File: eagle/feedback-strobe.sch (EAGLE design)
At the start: 17 parts, among them J2 MOTOR, U1 74LCX760SOIC20, U2 +12v, U3 V_REG_317SMD

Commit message: finished v1 PCB design
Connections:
- net GND: now also U1./OE1, U1./OE2
- net LED1: now also R4.2; no longer R1.2
- net LED2: now also R3.2; no longer R2.2
- net LED3: now also R2.2; no longer R3.2
- net LED4: now also R1.2; no longer R4.2
- net LED5: now also R8.2; no longer R5.2
- net LED6: now also R7.2; no longer R6.2
- net LED7: now also R6.2; no longer R7.2
- net LED8: now also R5.2; no longer R8.2
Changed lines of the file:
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@@
 <part name="C1" library="SparkFun-Passives" deviceset="CAP_POL" device="F80" value="220uF"/>
 <part name="GND3" library="SparkFun-Aesthetics" deviceset="GND" device=""/>
+<part name="GND4" library="SparkFun-Aesthetics" deviceset="GND" device=""/>
+<part name="GND5" library="SparkFun-Aesthetics" deviceset="GND" device=""/>
 </parts>
 <sheets>
@@
 <instance part="C1" gate="G$1" x="5.08" y="116.84"/>
 <instance part="GND3" gate="1" x="-35.56" y="104.14"/>
+<instance part="GND4" gate="1" x="-2.54" y="116.84"/>
+<instance part="GND5" gate="1" x="76.2" y="104.14"/>
 </instances>
 <busses>
@@
 <wire x1="15.24" y1="119.38" x2="15.24" y2="109.22" width="0.1524" layer="91"/>
 <wire x1="15.24" y1="109.22" x2="5.08" y2="109.22" width="0.1524" layer="91"/>
-<pinref part="DC_IN" gate="G$1" pin="GNDBREAK"/>
 <pinref part="DC_IN" gate="G$1" pin="GND"/>
-<wire x1="5.08" y1="109.22" x2="0" y2="109.22" width="0.1524" layer="91"/>
-<wire x1="-10.16" y1="124.46" x2="-10.16" y2="121.92" width="0.1524" layer="91"/>
-<wire x1="-10.16" y1="121.92" x2="0" y2="121.92" width="0.1524" layer="91"/>
-<wire x1="0" y1="121.92" x2="0" y2="109.22" width="0.1524" layer="91"/>
-<junction x="0" y="109.22"/>
+<wire x1="5.08" y1="109.22" x2="-7.62" y2="109.22" width="0.1524" layer="91"/>
+<wire x1="-10.16" y1="121.92" x2="-7.62" y2="121.92" width="0.1524" layer="91"/>
+<wire x1="-7.62" y1="121.92" x2="-7.62" y2="109.22" width="0.1524" layer="91"/>
+<junction x="-7.62" y="109.22"/>
 <pinref part="C1" gate="G$1" pin="-"/>
 <wire x1="5.08" y1="111.76" x2="5.08" y2="109.22" width="0.1524" layer="91"/>
 <junction x="5.08" y="109.22"/>
 <pinref part="GND3" gate="1" pin="GND"/>
-<wire x1="0" y1="109.22" x2="-35.56" y2="109.22" width="0.1524" layer="91"/>
+<wire x1="-7.62" y1="109.22" x2="-35.56" y2="109.22" width="0.1524" layer="91"/>
 <wire x1="-35.56" y1="109.22" x2="-35.56" y2="106.68" width="0.1524" layer="91"/>
 </segment>
@@
 <pinref part="GND2" gate="1" pin="GND"/>
 <wire x1="27.94" y1="73.66" x2="27.94" y2="68.58" width="0.1524" layer="91"/>
+</segment>
+<segment>
+<pinref part="DC_IN" gate="G$1" pin="GNDBREAK"/>
+<pinref part="GND4" gate="1" pin="GND"/>
+<wire x1="-10.16" y1="124.46" x2="-2.54" y2="124.46" width="0.1524" layer="91"/>
+<wire x1="-2.54" y1="124.46" x2="-2.54" y2="119.38" width="0.1524" layer="91"/>
+</segment>
+<segment>
+<pinref part="U1" gate="U1" pin="/OE2"/>
+<wire x1="58.42" y1="93.98" x2="68.58" y2="93.98" width="0.1524" layer="91"/>
+<wire x1="68.58" y1="93.98" x2="68.58" y2="111.76" width="0.1524" layer="91"/>
+<wire x1="68.58" y1="111.76" x2="25.4" y2="111.76" width="0.1524" layer="91"/>
+<wire x1="25.4" y1="111.76" x2="25.4" y2="99.06" width="0.1524" layer="91"/>
+<pinref part="U1" gate="U1" pin="/OE1"/>
+<wire x1="25.4" y1="99.06" x2="27.94" y2="99.06" width="0.1524" layer="91"/>
+<wire x1="68.58" y1="111.76" x2="76.2" y2="111.76" width="0.1524" layer="91"/>
+<wire x1="76.2" y1="111.76" x2="76.2" y2="106.68" width="0.1524" layer="91"/>
+<pinref part="GND5" gate="1" pin="GND"/>
 </segment>
 </net>
@@
 <net name="LED1" class="0">
 <segment>
-<pinref part="R1" gate="G$1" pin="2"/>
-<wire x1="-22.86" y1="81.28" x2="-7.62" y2="81.28" width="0.1524" layer="91"/>
-</segment>
-<segment>
 <pinref part="U1" gate="U1" pin="O_0"/>
 <wire x1="58.42" y1="91.44" x2="63.5" y2="91.44" width="0.1524" layer="91"/>
 <label x="63.5" y="91.44" size="1.778" layer="95"/>
 </segment>
+<segment>
+<pinref part="R4" gate="G$1" pin="2"/>
+<wire x1="-12.7" y1="73.66" x2="-7.62" y2="73.66" width="0.1524" layer="91"/>
+</segment>
 </net>
 <net name="N$3" class="0">
@@
 <net name="LED2" class="0">
 <segment>
-<pinref part="R2" gate="G$1" pin="2"/>
-<wire x1="-12.7" y1="78.74" x2="-7.62" y2="78.74" width="0.1524" layer="91"/>
-</segment>
-<segment>
 <pinref part="U1" gate="U1" pin="O_1"/>
 <wire x1="58.42" y1="86.36" x2="63.5" y2="86.36" width="0.1524" layer="91"/>
 <label x="63.5" y="86.36" size="1.778" layer="95"/>
 </segment>
+<segment>
+<pinref part="R3" gate="G$1" pin="2"/>
+<wire x1="-22.86" y1="76.2" x2="-7.62" y2="76.2" width="0.1524" layer="91"/>
+</segment>
 </net>
 <net name="N$5" class="0">
@@
 <net name="LED3" class="0">
 <segment>
-<pinref part="R3" gate="G$1" pin="2"/>
-<wire x1="-22.86" y1="76.2" x2="-7.62" y2="76.2" width="0.1524" layer="91"/>
-</segment>
-<segment>
 <pinref part="U1" gate="U1" pin="O_2"/>
 <wire x1="58.42" y1="81.28" x2="63.5" y2="81.28" width="0.1524" layer="91"/>
 <label x="63.5" y="81.28" size="1.778" layer="95"/>
 </segment>
+<segment>
+<pinref part="R2" gate="G$1" pin="2"/>
+<wire x1="-12.7" y1="78.74" x2="-7.62" y2="78.74" width="0.1524" layer="91"/>
+</segment>
 </net>
 <net name="LED4" class="0">
-<segment>
-<pinref part="R4" gate="G$1" pin="2"/>
-<wire x1="-12.7" y1="73.66" x2="-7.62" y2="73.66" width="0.1524" layer="91"/>
-</segment>
 <segment>
 <pinref part="U1" gate="U1" pin="O_3"/>
@@
 <label x="63.5" y="76.2" size="1.778" layer="95"/>
 </segment>
+<segment>
+<pinref part="R1" gate="G$1" pin="2"/>
+<wire x1="-22.86" y1="81.28" x2="-7.62" y2="81.28" width="0.1524" layer="91"/>
+</segment>
 </net>
 <net name="LED6" class="0">
-<segment>
-<pinref part="R6" gate="G$1" pin="2"/>
-<wire x1="-12.7" y1="68.58" x2="-7.62" y2="68.58" width="0.1524" layer="91"/>
-</segment>
 <segment>
 <pinref part="U1" gate="U1" pin="O_5"/>
@@
 <label x="17.78" y="88.9" size="1.778" layer="95"/>
 </segment>
+<segment>
+<pinref part="R7" gate="G$1" pin="2"/>
+<wire x1="-22.86" y1="66.04" x2="-7.62" y2="66.04" width="0.1524" layer="91"/>
+</segment>
 </net>
 <net name="LED8" class="0">
-<segment>
-<pinref part="R8" gate="G$1" pin="2"/>
-<wire x1="-12.7" y1="63.5" x2="-7.62" y2="63.5" width="0.1524" layer="91"/>
-</segment>
 <segment>
 <pinref part="U1" gate="U1" pin="O_7"/>
@@
 <label x="17.78" y="78.74" size="1.778" layer="95"/>
 </segment>
+<segment>
+<pinref part="R5" gate="G$1" pin="2"/>
+<wire x1="-22.86" y1="71.12" x2="-7.62" y2="71.12" width="0.1524" layer="91"/>
+</segment>
 </net>
 <net name="N$12" class="0">
@@
 <net name="LED7" class="0">
 <segment>
-<pinref part="R7" gate="G$1" pin="2"/>
-<wire x1="-22.86" y1="66.04" x2="-7.62" y2="66.04" width="0.1524" layer="91"/>
-</segment>
-<segment>
 <pinref part="U1" gate="U1" pin="O_6"/>
 <wire x1="22.86" y1="83.82" x2="27.94" y2="83.82" width="0.1524" layer="91"/>
 <label x="17.78" y="83.82" size="1.778" layer="95"/>
 </segment>
+<segment>
+<pinref part="R6" gate="G$1" pin="2"/>
+<wire x1="-12.7" y1="68.58" x2="-7.62" y2="68.58" width="0.1524" layer="91"/>
+</segment>
 </net>
 <net name="LED5" class="0">
-<segment>
-<pinref part="R5" gate="G$1" pin="2"/>
-<wire x1="-7.62" y1="71.12" x2="-22.86" y2="71.12" width="0.1524" layer="91"/>
-</segment>
 <segment>
 <pinref part="U1" gate="U1" pin="O_4"/>
@@
 <label x="17.78" y="93.98" size="1.778" layer="95"/>
 </segment>
-</net>
+<segment>
+<pinref part="R8" gate="G$1" pin="2"/>
+<wire x1="-12.7" y1="63.5" x2="-7.62" y2="63.5" width="0.1524" layer="91"/>
+</segment>
+</net>

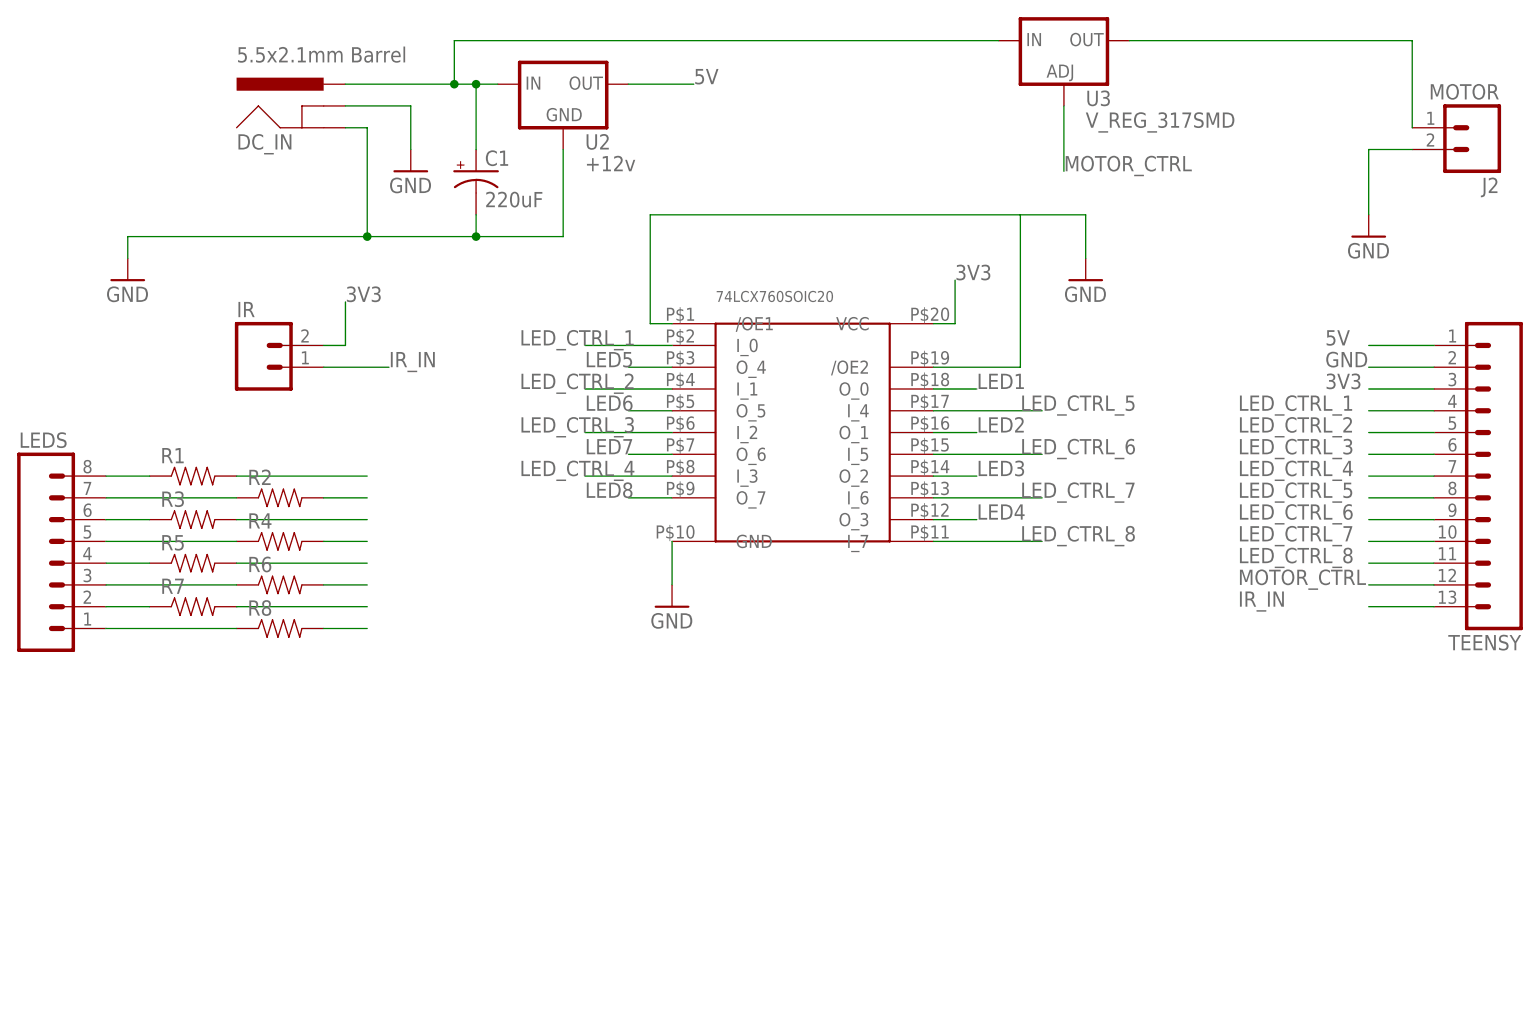
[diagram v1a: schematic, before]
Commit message: edited mosfet label
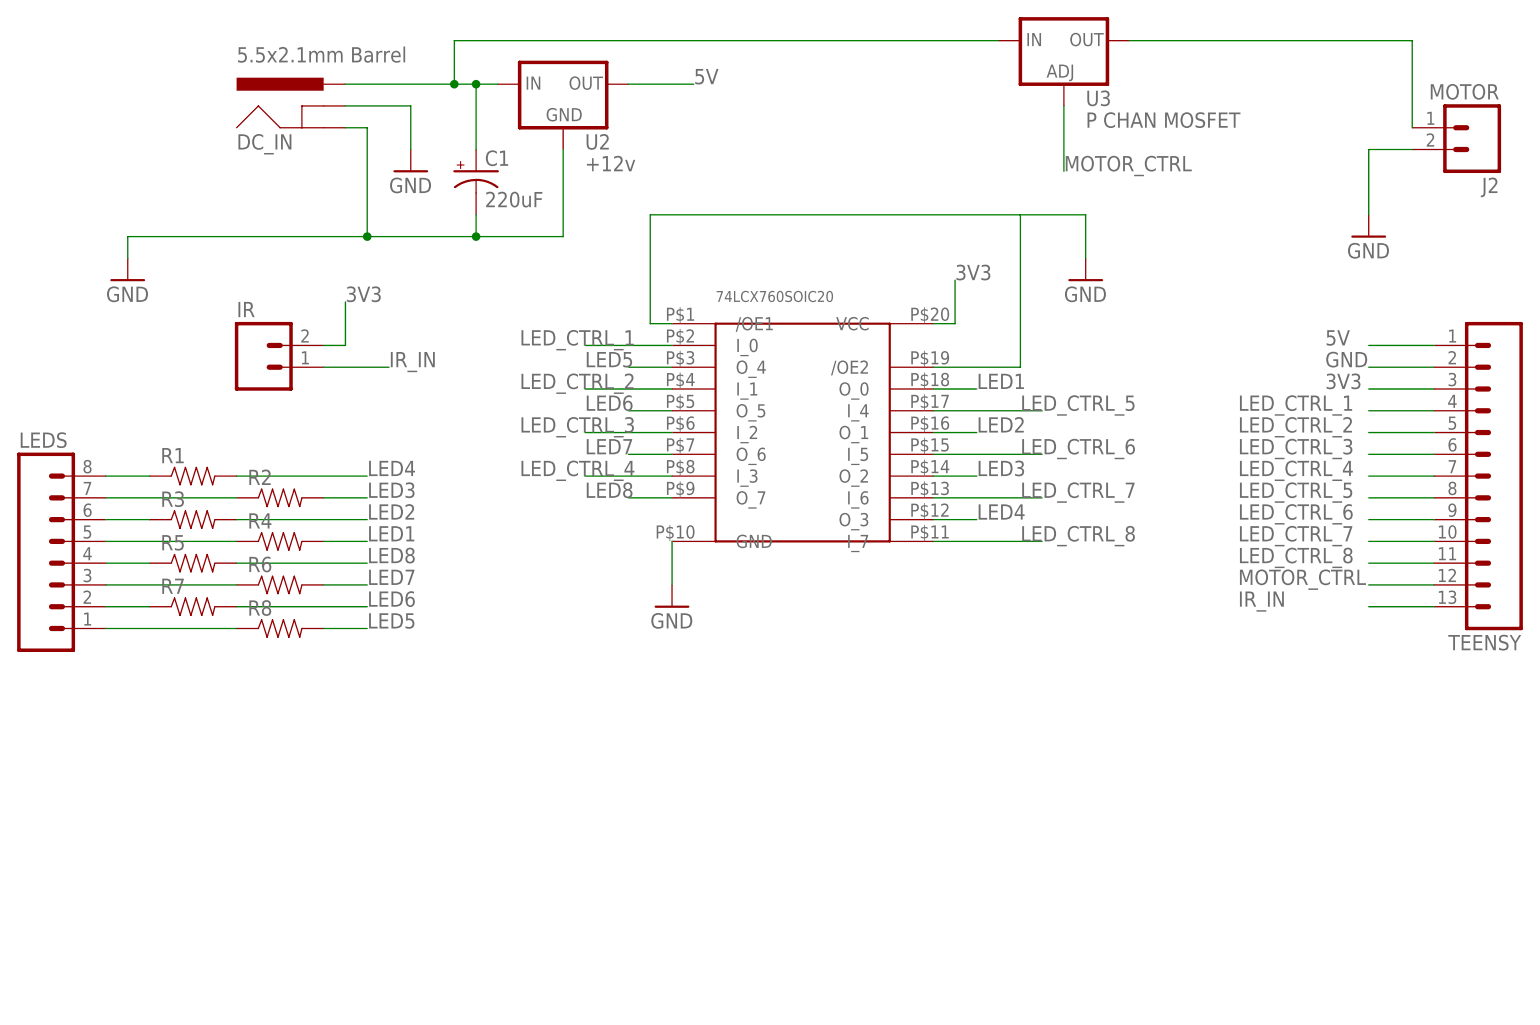
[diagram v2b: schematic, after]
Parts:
- U3: value V_REG_317SMD -> P CHAN MOSFET
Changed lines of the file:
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@@
 <part name="U1" library="SparkFun-DigitalIC" deviceset="74LCX760" device="SOIC20"/>
 <part name="U2" library="SparkFun-PowerIC" deviceset="V_REG_78XX" device="7812" value="+12v"/>
-<part name="U3" library="SparkFun-PowerIC" deviceset="V_REG_317" device="SMD"/>
+<part name="U3" library="SparkFun-PowerIC" deviceset="V_REG_317" device="SMD" value="P CHAN MOSFET"/>
 <part name="GND1" library="SparkFun-Aesthetics" deviceset="GND" device=""/>
 <part name="TEENSY" library="SparkFun-Connectors" deviceset="M13" device=""/>
@@
 <pinref part="R4" gate="G$1" pin="2"/>
 <wire x1="-12.7" y1="73.66" x2="-7.62" y2="73.66" width="0.1524" layer="91"/>
+<label x="-7.62" y="73.66" size="1.778" layer="95"/>
 </segment>
 </net>
@@
 <pinref part="R3" gate="G$1" pin="2"/>
 <wire x1="-22.86" y1="76.2" x2="-7.62" y2="76.2" width="0.1524" layer="91"/>
+<label x="-7.62" y="76.2" size="1.778" layer="95"/>
 </segment>
 </net>
@@
 <pinref part="R2" gate="G$1" pin="2"/>
 <wire x1="-12.7" y1="78.74" x2="-7.62" y2="78.74" width="0.1524" layer="91"/>
+<label x="-7.62" y="78.74" size="1.778" layer="95"/>
 </segment>
 </net>
@@
 <pinref part="R1" gate="G$1" pin="2"/>
 <wire x1="-22.86" y1="81.28" x2="-7.62" y2="81.28" width="0.1524" layer="91"/>
+<label x="-7.62" y="81.28" size="1.778" layer="95"/>
 </segment>
 </net>
@@
 <pinref part="R7" gate="G$1" pin="2"/>
 <wire x1="-22.86" y1="66.04" x2="-7.62" y2="66.04" width="0.1524" layer="91"/>
+<label x="-7.62" y="66.04" size="1.778" layer="95"/>
 </segment>
 </net>
@@
 <pinref part="R5" gate="G$1" pin="2"/>
 <wire x1="-22.86" y1="71.12" x2="-7.62" y2="71.12" width="0.1524" layer="91"/>
+<label x="-7.62" y="71.12" size="1.778" layer="95"/>
 </segment>
 </net>
@@
 <pinref part="R6" gate="G$1" pin="2"/>
 <wire x1="-12.7" y1="68.58" x2="-7.62" y2="68.58" width="0.1524" layer="91"/>
+<label x="-7.62" y="68.58" size="1.778" layer="95"/>
 </segment>
 </net>
@@
 <pinref part="R8" gate="G$1" pin="2"/>
 <wire x1="-12.7" y1="63.5" x2="-7.62" y2="63.5" width="0.1524" layer="91"/>
-</segment>
-</net>
+<label x="-7.62" y="63.5" size="1.778" layer="95"/>
+</segment>
+</net>

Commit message: new components added, new board dimensions set. routing started. mosfet footprint from digikey not wanting to connect nets
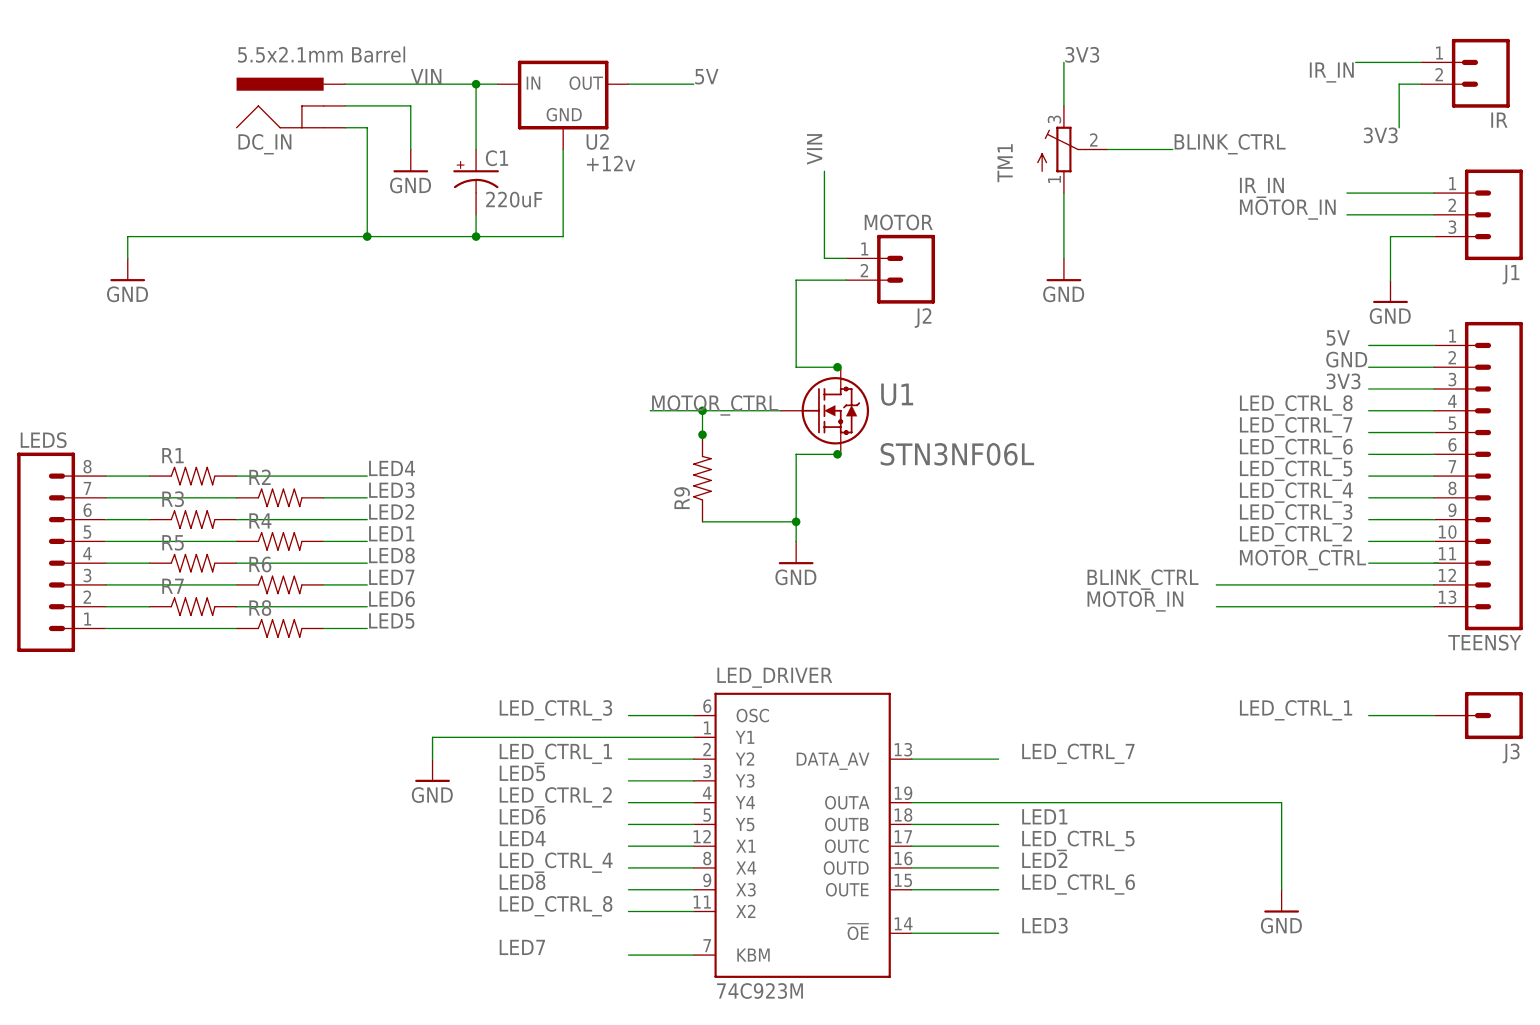
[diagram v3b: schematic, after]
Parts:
- removed U3: P CHAN MOSFET, SparkFun-PowerIC:V_REG_317SMD
- added J1: (no value), SparkFun-Connectors:M03PTH
- added J3: (no value), SparkFun-Connectors:M01PTH
- added LED_DRIVER: 74C923M, 74xx-us:74C923M
- added R9: (no value), SparkFun-Passives:RESISTOR0603-RES
- added TM1: (no value), adafruit:TRIMPOT3386
- U1: value 74LCX760SOIC20 -> STN3NF06L; device SparkFun-DigitalIC:74LCX760SOIC20 -> n-fet:STN3NF06L
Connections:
- removed net N$11: C1.+, DC_IN.PWR, U2.IN, U3.IN
- removed net N$9: J2.1, U3.OUT
- new net BLINK_CTRL: TEENSY.12, TM1.S
- new net MOTOR_IN: J1.2, TEENSY.13
- new net N$8: J2.2
- new net VIN: C1.+, DC_IN.PWR, J2.1, U2.IN
- net 3V3: now also TM1.E; no longer U1.VCC
- net GND: now also J1.3, LED_DRIVERG$1.OUTA, LED_DRIVERG$1.Y1, R9.1, TM1.A; no longer J2.2, U1./OE1, U1./OE2, U1.GND
- net IR_IN: now also J1.1; no longer TEENSY.13
- net LED1: now also LED_DRIVERG$1.OUTB; no longer U1.O_0
- net LED2: now also LED_DRIVERG$1.OUTD; no longer U1.O_1
- net LED3: now also LED_DRIVERG$1.!OE; no longer U1.O_2
- net LED4: now also LED_DRIVERG$1.X1; no longer U1.O_3
- net LED5: now also LED_DRIVERG$1.Y3; no longer U1.O_4
- net LED6: now also LED_DRIVERG$1.Y5; no longer U1.O_5
- net LED7: now also LED_DRIVERG$1.KBM; no longer U1.O_6
- net LED8: now also LED_DRIVERG$1.X3; no longer U1.O_7
- net LED_CTRL_1: now also J3.1, LED_DRIVERG$1.Y2; no longer TEENSY.4, U1.I_0
- net LED_CTRL_2: now also LED_DRIVERG$1.Y4, TEENSY.10; no longer TEENSY.5, U1.I_1
- net LED_CTRL_3: now also LED_DRIVERG$1.OSC, TEENSY.9; no longer TEENSY.6, U1.I_2
- net LED_CTRL_4: now also LED_DRIVERG$1.X4, TEENSY.8; no longer TEENSY.7, U1.I_3
- net LED_CTRL_5: now also LED_DRIVERG$1.OUTC, TEENSY.7; no longer TEENSY.8, U1.I_4
- net LED_CTRL_6: now also LED_DRIVERG$1.OUTE, TEENSY.6; no longer TEENSY.9, U1.I_5
- net LED_CTRL_7: now also LED_DRIVERG$1.DATA_AV, TEENSY.5; no longer TEENSY.10, U1.I_6
- net LED_CTRL_8: now also LED_DRIVERG$1.X2, TEENSY.4; no longer TEENSY.11, U1.I_7
- net MOTOR_CTRL: now also R9.2, U1.1; no longer TEENSY.12, U3.ADJ
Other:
- moved on the sheet: IR, J2
